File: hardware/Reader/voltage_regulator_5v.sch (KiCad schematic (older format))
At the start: 5 parts

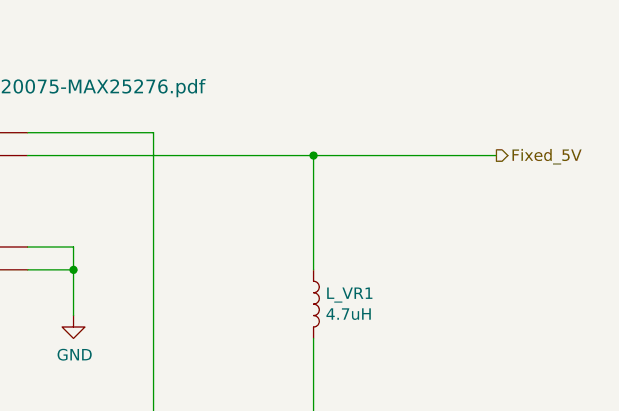
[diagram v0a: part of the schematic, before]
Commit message: Fixed numerous bugs in design for Reader Schematic and PCB
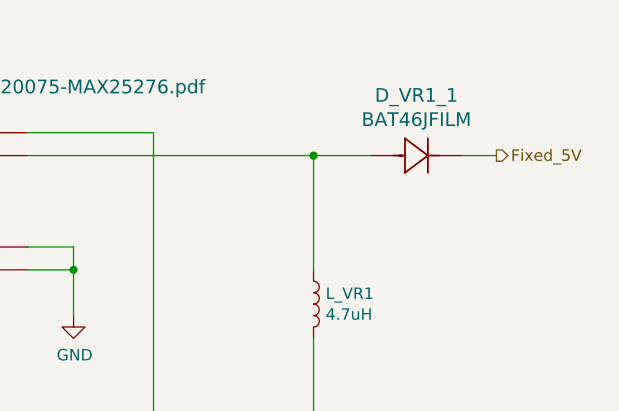
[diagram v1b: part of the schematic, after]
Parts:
- added D_VR1_1: BAT46JFILM, footprints:BAT46JFILM, symbol BAT46:BAT46
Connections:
- net Fixed_5V: now also D_VR1_1.1; no longer L_VR1.1, U_VR1.9 (OUT)
- new net: D_VR1_1.2, L_VR1.1, U_VR1.9 (OUT)
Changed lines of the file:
@@
 $Descr USLetter 11000 8500
 encoding utf-8
-Sheet 18 19
+Sheet 16 19
 Title "CANnect Reader | Voltage Regulator (5V)"
 Date "2020-11-19"
@@
 Wire Wire Line
 	6650 2800 6650 2300
-Connection ~ 6650 2300
-Wire Wire Line
-	6650 2300 7450 2300
 $Comp
 L Device:C C_VR1_2
@@
 Wire Wire Line
 	2700 2150 2950 2150
+$Comp
+L BAT46:BAT46 D_VR1_1
+U 1 1 5FB92426
+P 6900 2300
+F 0 "D_VR1_1" H 7100 2563 60  0000 C CNN
+F 1 "BAT46JFILM" H 7100 2457 60  0000 C CNN
+F 2 "footprints:BAT46JFILM" H 7100 1940 60  0001 C CNN
+F 3 "https://www.st.com/content/ccc/resource/technical/document/datasheet/c6/32/d4/4a/28/d3/4b/11/CD00004930.pdf/files/CD00004930.pdf/jcr:content/translations/en.CD00004930.pdf" H 7100 2457 60  0001 C CNN
+F 4 "STMicroelectronics" H 6900 2300 50  0001 C CNN "Manufacturer"
+F 5 "BAT46JFILM" H 6900 2300 50  0001 C CNN "Part Name"
+F 6 "DigiKey Canada" H 6900 2300 50  0001 C CNN "Vendor"
+F 7 "497-6653-1-ND" H 6900 2300 50  0001 C CNN "digikeypn"
+	1    6900 2300
+	1    0    0    -1
+$EndComp
+Wire Wire Line
+	6650 2300 6900 2300
+Connection ~ 6650 2300
+Wire Wire Line
+	7300 2300 7450 2300
 $EndSCHEMATC

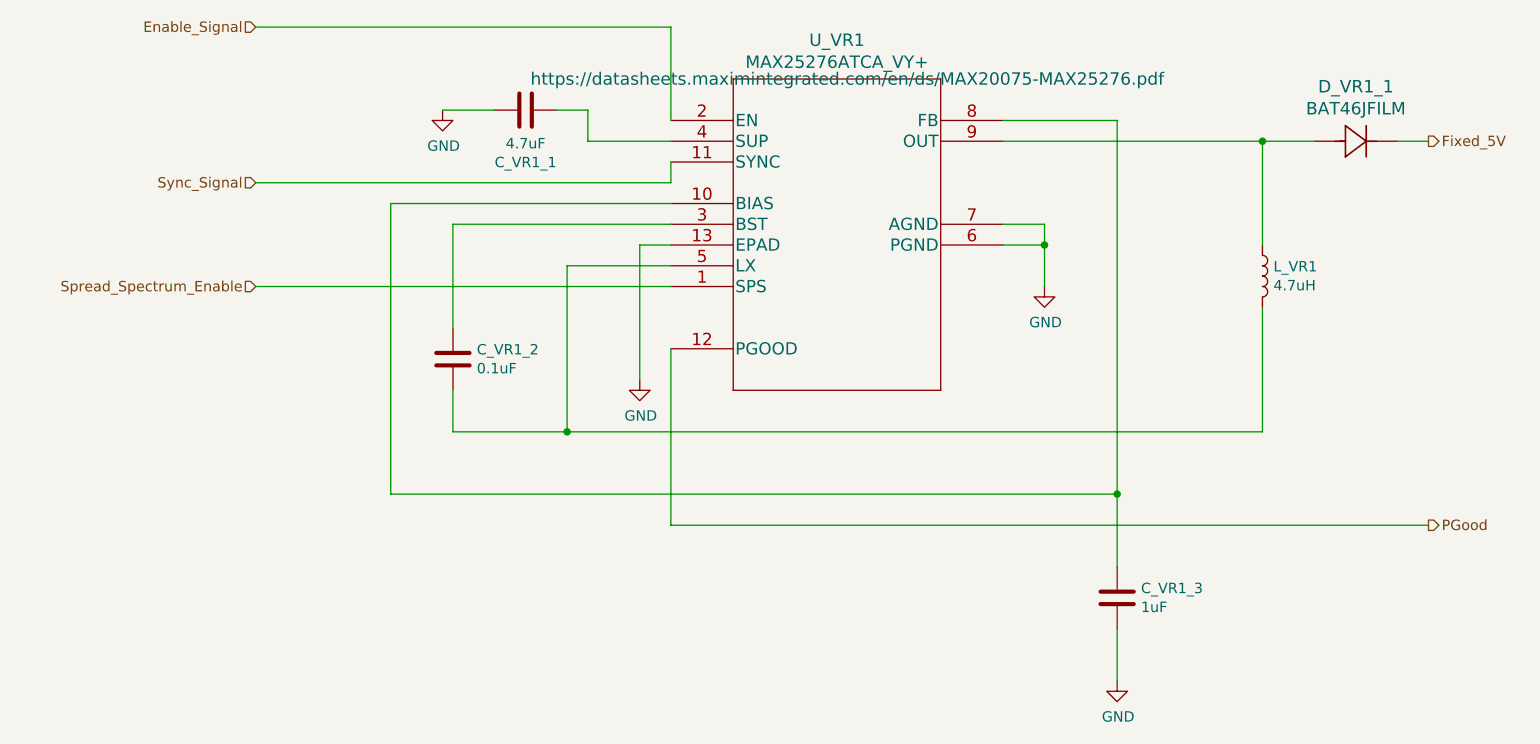
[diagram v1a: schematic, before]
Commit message: Updated reader schematic to v0.0.5 by adding ESP32, removing unused transceivers, fixed design flaws, increased header pins and fixed footprints. Working on reader PCB design
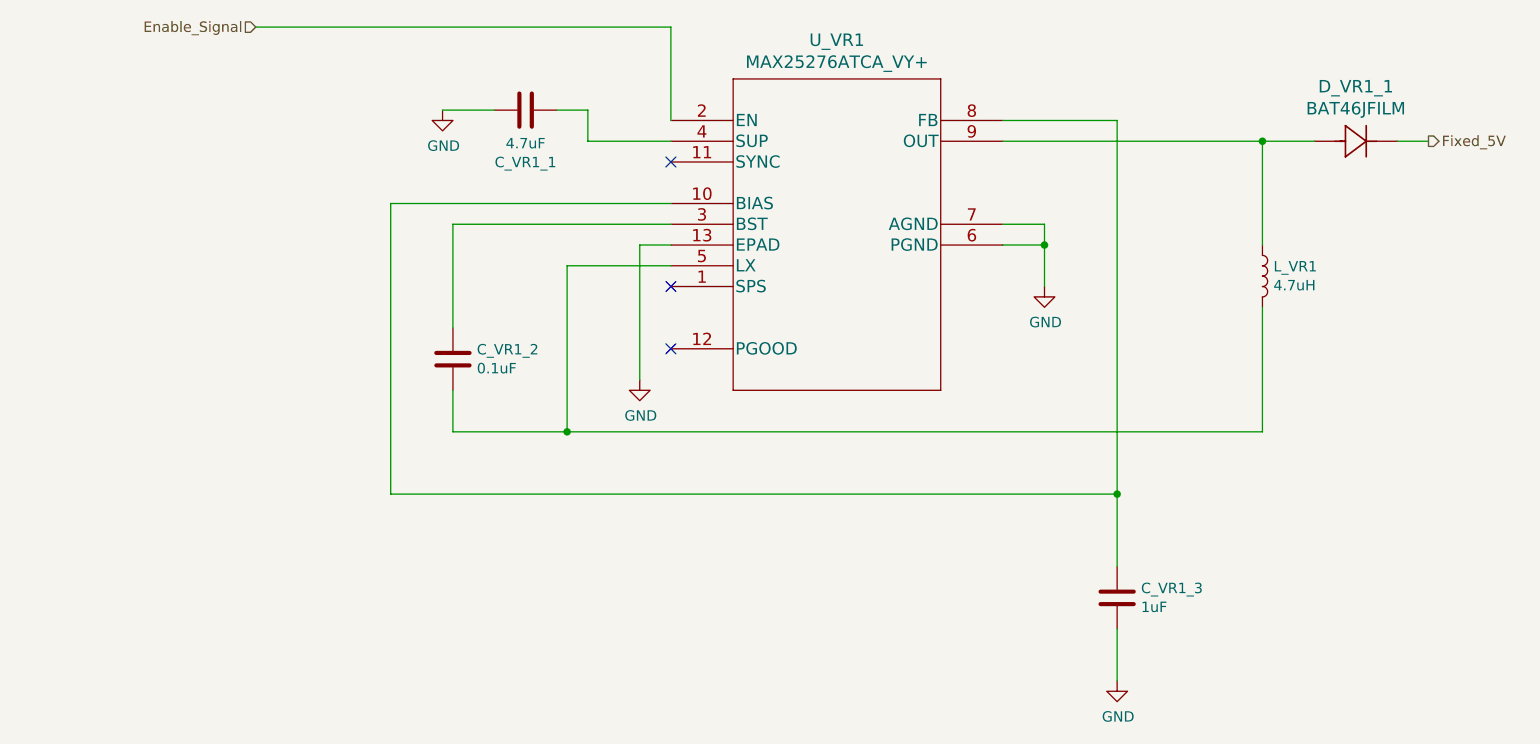
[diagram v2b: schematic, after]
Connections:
- net PGood: no longer names the net of U_VR1.12 (PGOOD)
- net Spread_Spectrum_Enable: no longer names the net of U_VR1.1 (SPS)
- net Sync_Signal: no longer names the net of U_VR1.11 (SYNC)
- no-connect marks 0 -> 3
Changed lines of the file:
@@
 $Descr USLetter 11000 8500
 encoding utf-8
-Sheet 16 19
+Sheet 7 17
 Title "CANnect Reader | Voltage Regulator (5V)"
-Date "2020-11-19"
+Date "2020-11-27"
 Rev "0.0.05"
 Comp "CANtech"
@@
 F 1 "MAX25276ATCA_VY+" H 4600 2481 60  0000 C CNN
 F 2 "footprints:MAX25276ATCA&slash_VY&plus_" H 4600 2440 60  0001 C CNN
-F 3 "https://datasheets.maximintegrated.com/en/ds/MAX20075-MAX25276.pdf" H 4650 2400 60  0000 C CNN
+F 3 "https://datasheets.maximintegrated.com/en/ds/MAX20075-MAX25276.pdf" H 4650 2400 60  0001 C CNN
 F 4 "MAX25276ATCA/VY+" H 3800 2200 50  0001 C CNN "Part Name"
 F 5 "Maxim Integrated" H 3800 2200 50  0001 C CNN "Manufacturer"
@@
 Text HLabel 1800 1750 0    50   Input ~ 0
 Enable_Signal
-Text HLabel 1800 2500 0    50   Input ~ 0
-Sync_Signal
 Text HLabel 7450 2300 2    50   Output ~ 0
 Fixed_5V
-Text HLabel 7450 4150 2    50   Output ~ 0
-PGood
 Wire Wire Line
 	5400 2300 6650 2300
@@
 Wire Wire Line
 	3800 1750 3800 2200
-Wire Wire Line
-	1800 2500 3800 2500
-Wire Wire Line
-	3800 2500 3800 2400
-Wire Wire Line
-	3800 3300 3800 4150
-Wire Wire Line
-	3800 4150 7450 4150
 $Comp
 L Device:L L_VR1
@@
 Wire Wire Line
 	3300 3700 6650 3700
-Text HLabel 1800 3000 0    50   Input ~ 0
-Spread_Spectrum_Enable
-Wire Wire Line
-	1800 3000 3800 3000
 $Comp
 L Device:C C_VR1_3
@@
 Wire Wire Line
 	7300 2300 7450 2300
+NoConn ~ 3800 2400
+NoConn ~ 3800 3000
+NoConn ~ 3800 3300
 $EndSCHEMATC

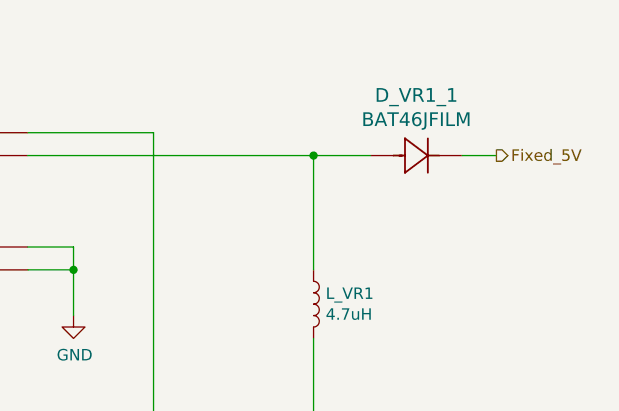
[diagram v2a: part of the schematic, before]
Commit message: Updated schematic and gerber to v0.0.05. Added ESP32. Removed MS CAN and SW CAN Transceivers. Added silkscreen text to header pins. Improved readability
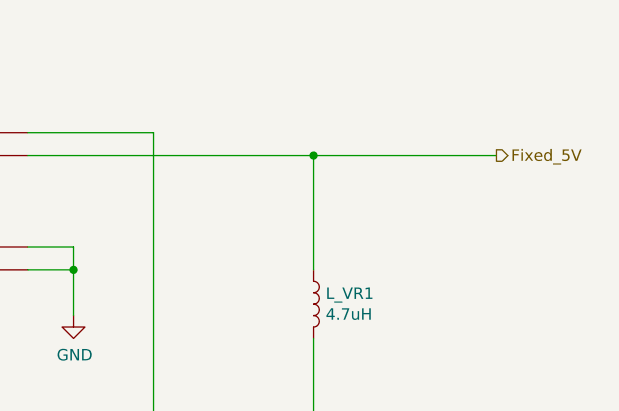
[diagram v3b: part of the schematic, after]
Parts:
- removed D_VR1_1: BAT46JFILM, footprints:BAT46JFILM, symbol BAT46:BAT46
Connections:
- net Fixed_5V: now also L_VR1.1, U_VR1.9 (OUT)
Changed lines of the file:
@@
 $Descr USLetter 11000 8500
 encoding utf-8
-Sheet 7 17
+Sheet 5 17
 Title "CANnect Reader | Voltage Regulator (5V)"
-Date "2020-11-27"
+Date "2020-11-29"
 Rev "0.0.05"
 Comp "CANtech"
@@
 Wire Wire Line
 	2700 2150 2950 2150
-$Comp
-L BAT46:BAT46 D_VR1_1
-U 1 1 5FB92426
-P 6900 2300
-F 0 "D_VR1_1" H 7100 2563 60  0000 C CNN
-F 1 "BAT46JFILM" H 7100 2457 60  0000 C CNN
-F 2 "footprints:BAT46JFILM" H 7100 1940 60  0001 C CNN
-F 3 "https://www.st.com/content/ccc/resource/technical/document/datasheet/c6/32/d4/4a/28/d3/4b/11/CD00004930.pdf/files/CD00004930.pdf/jcr:content/translations/en.CD00004930.pdf" H 7100 2457 60  0001 C CNN
-F 4 "STMicroelectronics" H 6900 2300 50  0001 C CNN "Manufacturer"
-F 5 "BAT46JFILM" H 6900 2300 50  0001 C CNN "Part Name"
-F 6 "DigiKey Canada" H 6900 2300 50  0001 C CNN "Vendor"
-F 7 "497-6653-1-ND" H 6900 2300 50  0001 C CNN "digikeypn"
-	1    6900 2300
-	1    0    0    -1
-$EndComp
-Wire Wire Line
-	6650 2300 6900 2300
 Connection ~ 6650 2300
-Wire Wire Line
-	7300 2300 7450 2300
 NoConn ~ 3800 2400
 NoConn ~ 3800 3000
 NoConn ~ 3800 3300
+Wire Wire Line
+	6650 2300 7450 2300
 $EndSCHEMATC
